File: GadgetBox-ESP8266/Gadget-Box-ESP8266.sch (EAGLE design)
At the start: 31 parts, among them U1 MCP73831T-2ACI/OT, U2 AP2112-3.3

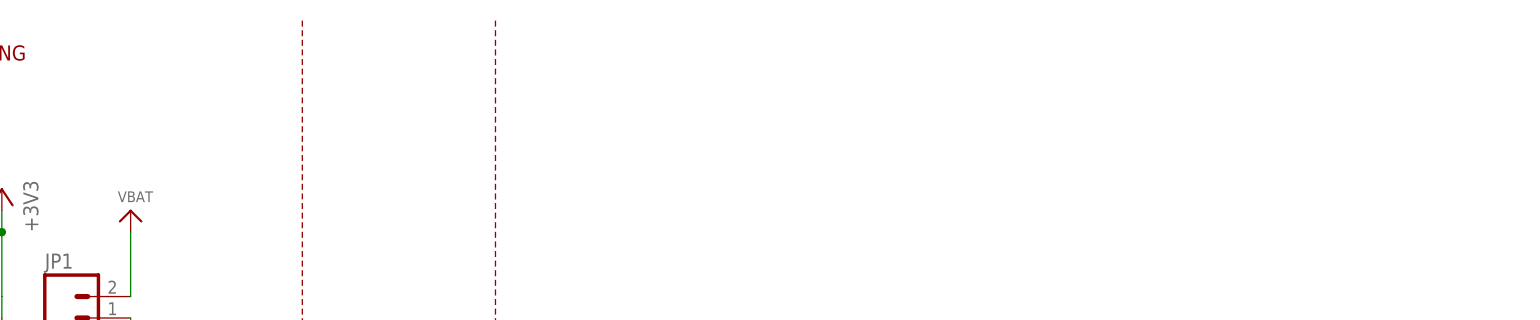
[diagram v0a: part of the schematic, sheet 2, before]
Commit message: Updated silkscreen and BOM for GadgetBox-ESP8266
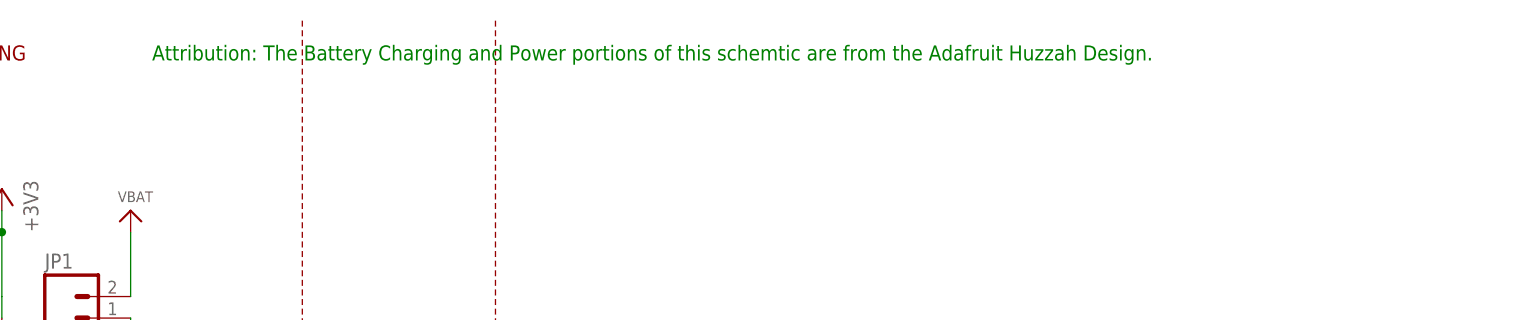
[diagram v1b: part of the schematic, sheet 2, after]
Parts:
- R10, R4: PARTNO RC0603JR-0710KL,YAGEO (VA),dk,311-10KGRCT-ND,RES SMD 10K OH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 -> RC0805JR-0710KL,YAGEO (VA),dk,311-10KARCT-ND,RES SMD 10K OH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
- R11, R12, R8, R9: PARTNO (none) -> RC0805JR-0710KL,YAGEO (VA),dk,311-10KARCT-ND,RES SMD 10K OH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
- R6: device GadgetFactory:R0603 -> GadgetFactory:R0805; PARTNO RC0603JR-0710KL,YAGEO (VA),dk,311-10KGRCT-ND,RES SMD 10K OH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 -> RC0805JR-0710KL,YAGEO (VA),dk,311-10KARCT-ND,RES SMD 10K OH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
- X2: PARTNO (none) -> 385646,AI-Thinker,dx.com,385646,ESP8266 Serial Wi-Fi Wirele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
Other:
- note added: "Attribution: The Battery Charging and Power portions of this schemtic are from the Adafruit Huzzah Design."
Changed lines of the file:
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@@
 </part>
 <part name="U$33" library="microbuilder" deviceset="GND" device=""/>
-<part name="R6" library="GadgetFactory" deviceset="R" device="0603" value="10K">
-<attribute name="PARTNO" value="RC0603JR-0710KL,YAGEO (VA),dk,311-10KGRCT-ND,RES SMD 10K OHM 5% 1/10W 0603 , REF36"/>
+<part name="R6" library="GadgetFactory" deviceset="R" device="0805" value="10K">
+<attribute name="PARTNO" value="RC0805JR-0710KL,YAGEO (VA),dk,311-10KARCT-ND,RES SMD 10K OHM 5% 1/8W 0805, REF63"/>
 </part>
 <part name="U$36" library="microbuilder" deviceset="GND" device=""/>
@@
 </part>
 <part name="R10" library="GadgetFactory" deviceset="R" device="0805" value="10K">
-<attribute name="PARTNO" value="RC0603JR-0710KL,YAGEO (VA),dk,311-10KGRCT-ND,RES SMD 10K OHM 5% 1/10W 0603 , REF36"/>
+<attribute name="PARTNO" value="RC0805JR-0710KL,YAGEO (VA),dk,311-10KARCT-ND,RES SMD 10K OHM 5% 1/8W 0805, REF63"/>
 </part>
 <part name="P+7" library="supply1" deviceset="VCC" device=""/>
@@
 <part name="X2" library="adafruit" deviceset="ESP-12" device="">
 <attribute name="ADAFRUIT" value="2491"/>
+<attribute name="PARTNO" value="385646,AI-Thinker,dx.com,385646,ESP8266 Serial Wi-Fi Wireless Transceiver Module - http://www.dx.com/p/esp-12e-esp8266-serial-wi-fi-wireless-transceiver-module-for-arduino-rpi-built-in-antenna-385646, REF94"/>
 </part>
 <part name="R8" library="GadgetFactory" deviceset="R" device="0805" value="10K">
 <attribute name="DIGIKEY" value="RMCF0805JT10K0CT-ND"/>
+<attribute name="PARTNO" value="RC0805JR-0710KL,YAGEO (VA),dk,311-10KARCT-ND,RES SMD 10K OHM 5% 1/8W 0805, REF63"/>
 </part>
 <part name="R9" library="GadgetFactory" deviceset="R" device="0805" value="10K">
 <attribute name="DIGIKEY" value="RMCF0805JT10K0CT-ND"/>
+<attribute name="PARTNO" value="RC0805JR-0710KL,YAGEO (VA),dk,311-10KARCT-ND,RES SMD 10K OHM 5% 1/8W 0805, REF63"/>
 </part>
 <part name="R11" library="GadgetFactory" deviceset="R" device="0805" value="10K">
 <attribute name="DIGIKEY" value="RMCF0805JT10K0CT-ND"/>
+<attribute name="PARTNO" value="RC0805JR-0710KL,YAGEO (VA),dk,311-10KARCT-ND,RES SMD 10K OHM 5% 1/8W 0805, REF63"/>
 </part>
 <part name="R12" library="GadgetFactory" deviceset="R" device="0805" value="10K">
 <attribute name="DIGIKEY" value="RMCF0805JT10K0CT-ND"/>
+<attribute name="PARTNO" value="RC0805JR-0710KL,YAGEO (VA),dk,311-10KARCT-ND,RES SMD 10K OHM 5% 1/8W 0805, REF63"/>
 </part>
 <part name="GND3" library="GadgetFactory" deviceset="GND" device=""/>
@@
 </part>
 <part name="R4" library="GadgetFactory" deviceset="R" device="0805" value="10K">
-<attribute name="PARTNO" value="RC0603JR-0710KL,YAGEO (VA),dk,311-10KGRCT-ND,RES SMD 10K OHM 5% 1/10W 0603 , REF36"/>
+<attribute name="PARTNO" value="RC0805JR-0710KL,YAGEO (VA),dk,311-10KARCT-ND,RES SMD 10K OHM 5% 1/8W 0805, REF63"/>
 </part>
 <part name="P+1" library="supply1" deviceset="VCC" device=""/>
@@
 <instance part="X2" gate="G$1" x="175.26" y="139.7">
 <attribute name="ADAFRUIT" x="175.26" y="139.7" size="1.778" layer="96" display="off"/>
+<attribute name="PARTNO" x="175.26" y="139.7" size="1.778" layer="96" display="off"/>
 </instance>
 <instance part="R8" gate="A" x="218.44" y="154.94" rot="R90">
 <attribute name="DIGIKEY" x="218.44" y="154.94" size="1.778" layer="96" rot="R90" display="off"/>
+<attribute name="PARTNO" x="218.44" y="154.94" size="1.778" layer="96" display="off"/>
 </instance>
 <instance part="R9" gate="A" x="205.74" y="116.84" rot="R90">
 <attribute name="DIGIKEY" x="205.74" y="116.84" size="1.778" layer="96" rot="R90" display="off"/>
+<attribute name="PARTNO" x="205.74" y="116.84" size="1.778" layer="96" display="off"/>
 </instance>
 <instance part="R11" gate="A" x="144.78" y="154.94" rot="R90">
 <attribute name="DIGIKEY" x="144.78" y="154.94" size="1.778" layer="96" rot="R90" display="off"/>
+<attribute name="PARTNO" x="144.78" y="154.94" size="1.778" layer="96" display="off"/>
 </instance>
 <instance part="R12" gate="A" x="149.86" y="154.94" rot="R90">
 <attribute name="DIGIKEY" x="149.86" y="154.94" size="1.778" layer="96" rot="R90" display="off"/>
+<attribute name="PARTNO" x="149.86" y="154.94" size="1.778" layer="96" display="off"/>
 </instance>
 <instance part="GND3" gate="A" x="205.74" y="109.22"/>
@@
 <wire x1="5.08" y1="71.12" x2="134.62" y2="71.12" width="0.1524" layer="94" style="shortdash"/>
 <text x="142.24" y="119.38" size="1.778" layer="94">Measure Battery (Populate R10 with 0 ohm jumper)</text>
+<text x="93.98" y="170.18" size="1.778" layer="91">Attribution: The Battery Charging and Power portions of this schemtic are from the Adafruit Huzzah Design.</text>
 </plain>
 <instances>
